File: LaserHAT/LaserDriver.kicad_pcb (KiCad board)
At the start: 2 copper layers, 65 x 56.9 mm, 69 parts, among them J1 GPIO, J2 Conn_02x02_Counter_Clockwise, J4 Jumper for 4-terminal diode c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, J5 USB_C_Receptacle_USB2.0_16P, J6 Conn_Coaxial, J7 Conn_Coaxial, Q1 SI3134KDWA-TP, Q2 DMN2056U, SW1 B, SW2 B, SW3 B, SW4 B, SW5 SW_SPDT, SW6 BSL, U1 CAT24C32, U2 MT3608, U3 TLV2371DBV, U4 MCP1700x-330xxMB, U5 AP2171W, U6 CH340N, U7 MSPM0G3507SRHBR

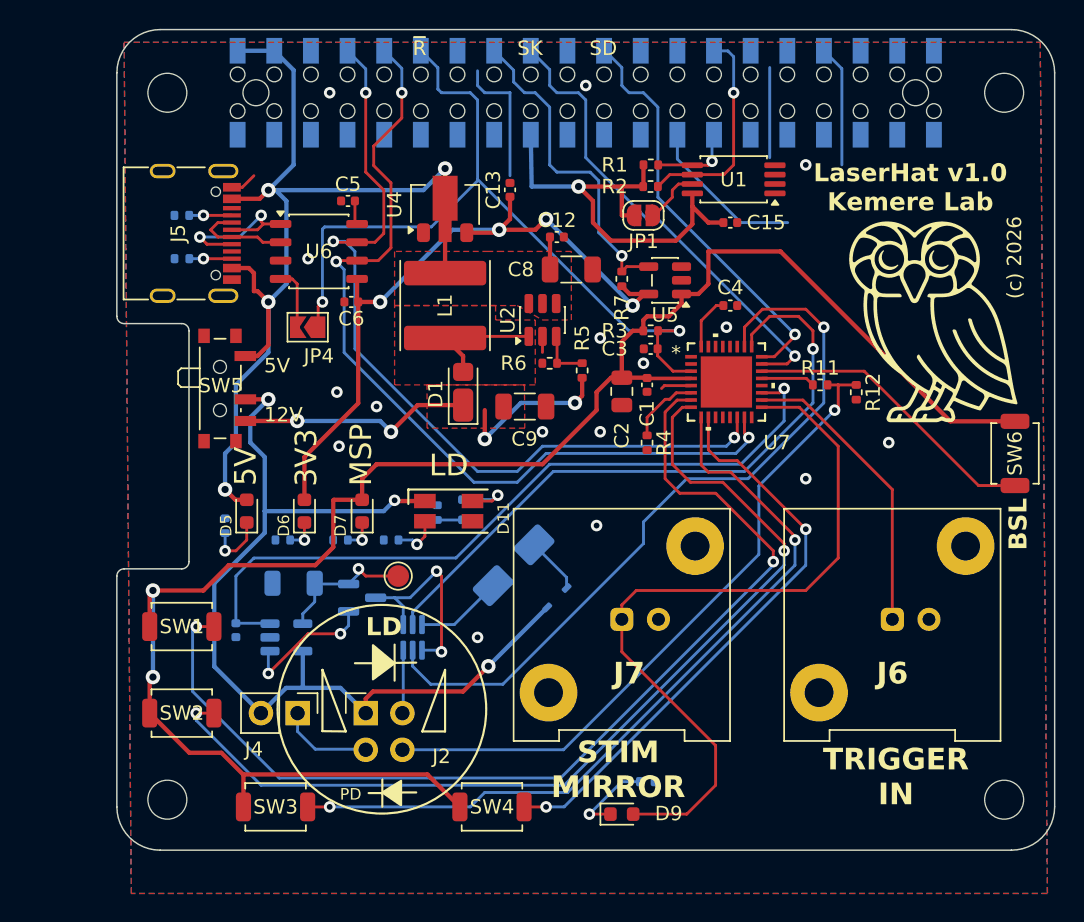
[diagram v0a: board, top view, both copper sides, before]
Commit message: LaserHAT Rev 2: hand-routed HAT, laser + e-stim daughterboards, fab outputs
HAT (LaserHAT/):
- Rev 1 -> Rev 2 schematic migration (tools/rev2_migrate.py): issue #3 fixes,
  OLED bonnet kept, analog stage moved to plug-in daughterboards (J8/J9),
  buffered BNC I/O, USB-C power switch + PFET ideal diode.
- MCU pin map re-optimised for fewest vias: Pi UART on UART1 (PA8/PA9), I2C on
  PA0/PA1 (fail-safe), PWM_A/B on TIMA0 CCP1/CCP3 (PA7/PA12) with FAULT0 on PA6,
  active-low buttons.  Pi header: SWD swapped, NRST <-> MCU_POWER_EN swapped.
- Stable symbol UUIDs so KiCad "Update PCB" never replaces footprints.
- PCB placed and routed by hand; tidied (tools/track_tidy.py), silkscreen
  decluttered (tools/silk_declutter.py).  DRC clean apart from known cosmetic items.
- JLC fab outputs regenerated (fab/LaserHAT).
- CLAUDE.md, REV2_NOTES.md updated; portable Claude memory in claude_memory/.

Daughterboards: LaserDaughter (300 mA laser driver) and EStimDaughter (isolated
e-stim, imported from kbest/estim_module); interface spec in estim_interface/.

Firmware/Pi: `make flash HAT_REV=2` selects the Rev 2 header wiring;
Pi/power_cycle.py takes its power/reset pins from the environment.

Co-Authored-By: Claude Opus 5.5 <noreply@anthropic.com>
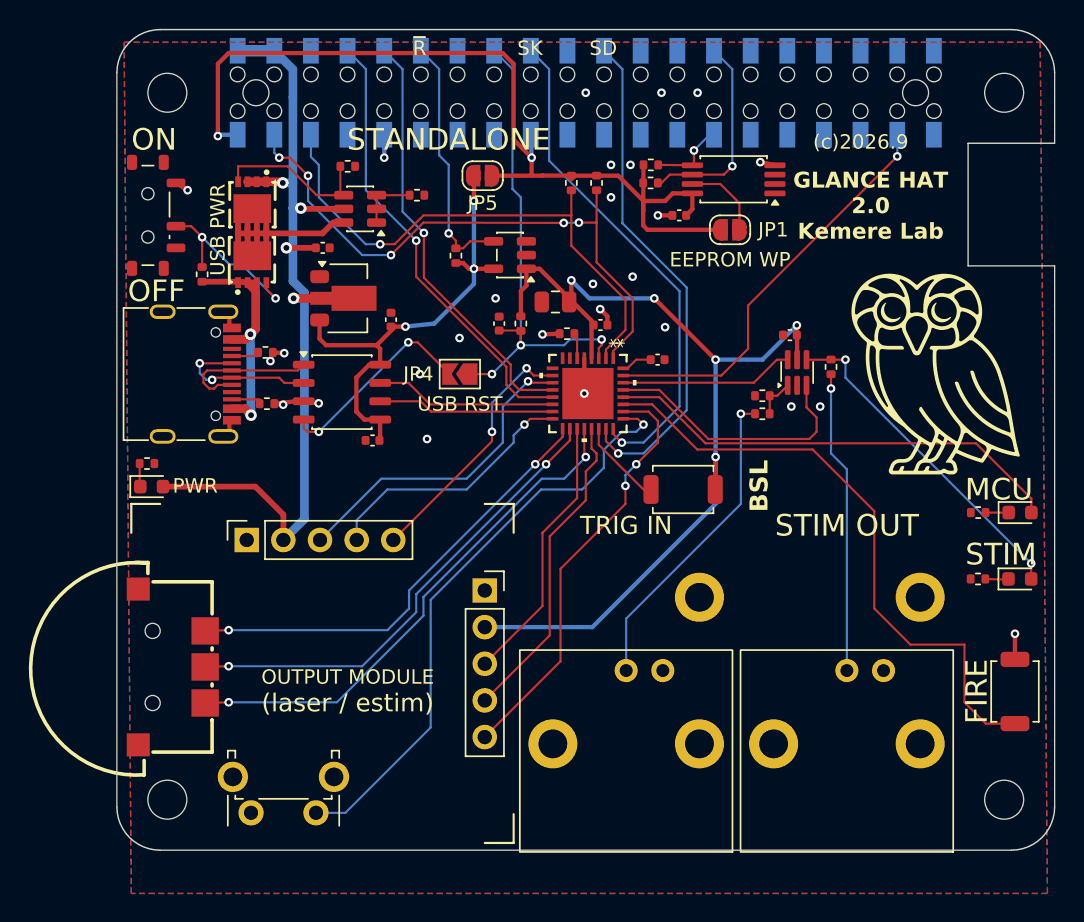
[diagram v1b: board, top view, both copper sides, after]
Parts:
- removed C11: 10nF, Capacitor_SMD:C_0402_1005Metric
- removed C5: 100nF, Capacitor_SMD:C_0402_1005Metric
- removed C8, C9: 22µF 16V, Capacitor_SMD:C_1206_3216Metric
- removed D1: SS14, Diode_SMD:D_SOD-123F
- removed D10: D_Zener 6.2V, Diode_SMD:D_SOD-523
- removed D11: LED_ABGR, LED_SMD:LED_RGB_1210
- removed D2: Zener 4.7V, 1.5W, Diode_SMD:D_SMA
- removed D3: 1N4148W, Footprints:D_SOD-323F
- removed D6: 3v3, Diode_SMD:D_0603_1608Metric
- removed J2: Conn_02x02_Counter_Clockwise, Connector_PinHeader_2.54mm:PinHeader_2x02_P2.54mm_Vertical
- removed J4: Jumper for 4-terminal diode configuration, Connector_PinHeader_2.54mm:PinHeader_1x02_P2.54mm_Vertical
- removed L1: 22uH, Inductor_SMD:L_APV_ANR6045
- removed Q2: DMN2056U, Package_TO_SOT_SMD:SOT-23
- removed R11: 1k 0.1%, Resistor_SMD:R_0402_1005Metric
- removed R12: 4.7k, Resistor_SMD:R_0402_1005Metric
- removed R14: 200, Resistor_SMD:R_0402_1005Metric
- removed R16: 470, Resistor_SMD:R_0402_1005Metric
- removed R17: 1k 1%, Resistor_SMD:R_0402_1005Metric
- removed R5: 187k 1%, Resistor_SMD:R_0402_1005Metric
- removed R6: 10k, Resistor_SMD:R_0402_1005Metric
- removed Rs1: 10Ω 1%, Resistor_SMD:R_1206_3216Metric
- removed SW1, SW3, SW4: B, Button_Switch_SMD:SW_SPST_TS-1088-xR020
- removed SW5: SW_SPDT, Button_Switch_SMD:SW_SPDT_PCM12
- removed TP1: TestPoint, TestPoint:TestPoint_Pad_D1.5mm
- removed U3: TLV2371DBV, Package_TO_SOT_SMD:SOT-23-5
- added C12: 100nF, Capacitor_SMD:C_0402_1005Metric, F.Cu at (114.3, 58.2)
- added J8: DB_POWER_TIMING, Connector_PinSocket_2.54mm:PinSocket_1x05_P2.54mm_Vertical, F.Cu at (109.0, 78.5)
- added J9: DB_ANALOG, Connector_PinSocket_2.54mm:PinSocket_1x05_P2.54mm_Vertical, F.Cu at (125.5, 82.0)
- added JP1: ID_WP, Jumper:SolderJumper-2_P1.3mm_Open_RoundedPad1.0x1.5mm, F.Cu at (142.5, 57.0)
- added Q3: AP30P30Q, Footprints:PDFN3333-8_PMOS_GSD, F.Cu at (109.4, 55.2)
- added Q5: AP30P30Q, Footprints:PDFN3333-8_PMOS_GSD, F.Cu at (109.4, 59.1)
- added R20: 4.7k, Resistor_SMD:R_0402_1005Metric, F.Cu at (131.5, 53.8)
- added R21: 47k, Resistor_SMD:R_0402_1005Metric, F.Cu at (120.8, 54.6)
- added R22: 10k, Resistor_SMD:R_0402_1005Metric, F.Cu at (116.0, 52.6)
- added R23: 1k, Resistor_SMD:R_0402_1005Metric, F.Cu at (144.7, 69.8)
- added R24: 100k, Resistor_SMD:R_0402_1005Metric, F.Cu at (144.7, 68.5)
- added R25: 33, Resistor_SMD:R_0402_1005Metric, F.Cu at (149.5, 66.5)
- added R26: 100k, Resistor_SMD:R_0402_1005Metric, F.Cu at (105.9, 60.1)
- added R3: 47k 1%, Resistor_SMD:R_0402_1005Metric, F.Cu at (128.0, 63.5)
- added SW10: USB PWR, Footprints:SW_SPDT_Shouhan_MSK12C02, F.Cu at (102.2, 56.0)
- added SW7: BL-DT (LCSC C53223909), Footprints:SW-SMD_BL-DT, F.Cu at (103.8, 87.3)
- added SW8: BACK, Button_Switch_THT:SW_Tactile_SPST_Angled_PTS645Vx39-2LFS, F.Cu at (113.8, 97.4)
- D7: value MSPM0 -> MCU
- J6: value Conn_Coaxial -> BNC TRIGGER IN; footprint Connector_Coaxial:BNC_Amphenol_031-5539_Vertical -> Footprints:BNC_Amphenol_031-5540_031-5539_Dual
- J7: value Conn_Coaxial -> BNC STIM OUT; footprint Connector_Coaxial:BNC_Amphenol_031-5539_Vertical -> Footprints:BNC_Amphenol_031-5540_031-5539_Dual
- JP4: value ID_WP -> RTS_NRST
- JP5: renamed from JP1; value ID_WP -> STANDALONE_3V3
- Q4: renamed from U2; value MT3608 -> DMMT5401
- R10, R8: moved to F.Cu
- R13: value 1k 1% -> 3k; moved to F.Cu
- R15: value 200 -> 2k; moved to F.Cu
- R18: value 470 -> 2k; moved to F.Cu
- R19: renamed from R3; value 47k 1% -> 4.7k
- SW9: renamed from SW2; value B -> FIRE
- U8: renamed from Q1; value SI3134KDWA-TP -> 74LVC2G17; moved to F.Cu
- moved SW9 57.8 mm to (162.2, 89.0), turned to 90 degrees
- moved D7 45.6 mm to (162.6, 76.6), turned to 0 degrees
- moved R15 44.2 mm to (159.7, 76.6)
- moved U8 32.4 mm to (147.2, 66.9)
- moved D9 32.0 mm to (162.6, 81.2)
- moved R18 26.9 mm to (159.7, 81.2), turned to 180 degrees
- moved SW6 23.1 mm to (139.2, 75.0), turned to 0 degrees
- moved J6 18.8 mm to (135.3, 87.5), turned to 180 degrees
- moved C16 17.5 mm to (146.7, 64.3), turned to 180 degrees
- moved J7 16.0 mm to (150.6, 87.5), turned to 180 degrees
- moved Q4 14.8 mm to (116.9, 55.5), turned to 180 degrees
- moved C13 12.2 mm to (119.0, 63.2)
- moved R10 11.6 mm to (110.4, 69.0), turned to 0 degrees
- moved R7 11.6 mm to (123.5, 58.8)
- moved JP5 11.5 mm to (125.3, 53.2), turned to 0 degrees
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- renumbered C12 to C16
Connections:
- net Net-(D9-K) renamed /BNC + Daughterboard I/O/STIM_LED_K
- C16 pad 1: +5V -> MSPM0_3V3
- C3 pad 1: /GPIO18/PCM.CLK -> /GPIO23
- D7 pad 2: MSPM0_3V3 -> LED_MCU
- D9 pad 2: /STIM_MIRROR -> /BNC + Daughterboard I/O/BUF_OUT
- J1 pad 10: /GPIO15/RXD0 -> PI_RXD
- J1 pad 3: /GPIO2/SDA1 -> I2C_SDA
- J1 pad 37: /GPIO26 -> PI_TRIGGER
- J1 pad 5: /GPIO3/SCL1 -> I2C_SCL
- J1 pad 8: /GPIO14/TXD0 -> PI_TXD
- J5 pad A4: +5V -> /USB-C UART/VBUS
- J5 pad A9: +5V -> /USB-C UART/VBUS
- J5 pad B4: +5V -> /USB-C UART/VBUS
- J5 pad B9: +5V -> /USB-C UART/VBUS
- J6 pad 1: /STIM_TRIGGER -> /BNC + Daughterboard I/O/BNC_IN
- J7 pad 1: /STIM_MIRROR -> /BNC + Daughterboard I/O/BNC_OUT
- JP4 pad 1: /GPIO18/PCM.CLK -> /GPIO23
- JP5 pad 1: Net-(JP1-A) -> +3V3
- Q4 pad 1: /Laser Driver Circuit/SW -> /USB-C UART/IDEAL_B
- Q4 pad 2: GND -> /USB-C UART/IDEAL_B
- Q4 pad 3: Net-(U2-FB) -> /USB-C UART/IDEAL_B
- Q4 pad 4: +5V -> /USB-C UART/IDEAL_G
- Q4 pad 6: unconnected-(U2-NC-Pad6) -> /USB-C UART/VBUS_SW
- R19 pad 1: MSPM0_3V3 -> RPi +3V3
- R19 pad 2: /GPIO18/PCM.CLK -> I2C_SDA
- R7 pad 2: /GPIO23 -> /GPIO18/PCM.CLK
- SW9 pad 1: /MSPM0 Controller/BUTTON2 -> /MSPM0 Controller/BUTTON5
- SW9 pad 2: MSPM0_3V3 -> GND
- U5 pad 4: /GPIO23 -> /GPIO18/PCM.CLK
- U6 pad 6: /GPIO15/RXD0 -> /MCU_UART_RX
- U6 pad 7: /GPIO14/TXD0 -> /MCU_UART_TX
- U6 pad 8: Net-(U6-V3) -> +3V3
- U7 pad 1: unconnected-(U7-PA0/FCC_IN-Pad1) -> I2C_SDA
- U7 pad 10: /MSPM0 Controller/BUTTON4 -> DB_GPIO
- U7 pad 11: unconnected-(U7-PA7/CLK_OUT-Pad11) -> DB_PWM_A
- U7 pad 12: unconnected-(U7-PA8-Pad12) -> PI_RXD
- U7 pad 13: unconnected-(U7-PA9/RTC_OUT/CLK_OUT-Pad13) -> PI_TXD
- U7 pad 14: /GPIO14/TXD0 -> /MCU_UART_TX
- U7 pad 15: /GPIO15/RXD0 -> /MCU_UART_RX
- U7 pad 16: unconnected-(U7-PA12/FCC_IN-Pad16) -> DB_PWM_B
- U7 pad 17: /STIM_MIRROR -> /MSPM0 Controller/BUTTON4
- U7 pad 18: /STIM_TRIGGER -> /MSPM0 Controller/BUTTON2
- U7 pad 19: /Laser Driver Circuit/LASER_VREF -> DB_DAC
- U7 pad 2: unconnected-(U7-PA1-Pad2) -> I2C_SCL
- U7 pad 20: unconnected-(U7-PA16/A1_1/FCC_IN-Pad20) -> /MSPM0 Controller/BUTTON3
- U7 pad 21: /Laser Driver Circuit/DIODE_ADC -> DB_ADC_A
- U7 pad 23: /GPIO24 -> /GPIO25
- U7 pad 24: /GPIO25 -> /GPIO24
- U7 pad 25: /Laser Driver Circuit/PWM_LASER -> /MSPM0 Controller/BUTTON1
- U7 pad 26: /Laser Driver Circuit/PWM_DUMMY -> DB_ADC_B
- U7 pad 27: unconnected-(U7-PA23/VREF+-Pad27) -> /MSPM0 Controller/BUTTON5
- U7 pad 28: unconnected-(U7-PA24/A0_3-Pad28) -> LED_MCU
- U7 pad 29: unconnected-(U7-PA25/A0_2/OPA0_IN1+-Pad29) -> MCU_STIM_OUT
- U7 pad 3: /GPIO18/PCM.CLK -> /GPIO23
- U7 pad 30: unconnected-(U7-PA26/A0_1-Pad30) -> MCU_STIM_IN
- U7 pad 31: unconnected-(U7-PA27/RTC_OUT/A0_0-Pad31) -> PI_TRIGGER
- U7 pad 33: unconnected-(U7-EPAD-Pad33) -> GND
- U7 pad 7: /MSPM0 Controller/BUTTON1 -> unconnected-(U7-PA3/COMP1_OUT/LFXIN-Pad7)
- U7 pad 8: /MSPM0 Controller/BUTTON2 -> unconnected-(U7-PA4/LFCLK_IN/LFXOUT-Pad8)
- U7 pad 9: /MSPM0 Controller/BUTTON3 -> unconnected-(U7-PA5/HFXIN/FCC_IN-Pad9)
- U8 pad 1: /Laser Driver Circuit/LaserDrive -> /BNC + Daughterboard I/O/BUF_IN
- U8 pad 2: /Laser Driver Circuit/PWM_DUMMY -> GND
- U8 pad 3: Net-(J2-LD_Cathode) -> MCU_STIM_OUT
- U8 pad 4: /Laser Driver Circuit/LaserDrive -> /BNC + Daughterboard I/O/BUF_OUT
- U8 pad 5: /Laser Driver Circuit/PWM_LASER -> MSPM0_3V3
- U8 pad 6: Net-(D2-K) -> MCU_STIM_IN
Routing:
- net LASER_V: track 66.0 -> 0.00 mm, vias 3 -> 0
- net /GPIO15/RXD0: track 60.9 -> 0.00 mm, vias 3 -> 0
- net /GPIO14/TXD0: track 58.3 -> 0.00 mm, vias 3 -> 0
- net MSPM0_3V3: track 123.9 -> 66.6 mm, vias 2 -> 5
- net /STIM_MIRROR: track 52.2 -> 0.00 mm
- net /Laser Driver Circuit/PWM_DUMMY: track 52.2 -> 0.00 mm, vias 1 -> 0
- net /Laser Driver Circuit/LASER_VREF: track 52.0 -> 0.00 mm, vias 1 -> 0
- net Net-(J2-PD_Anode): track 46.3 -> 0.00 mm, vias 1 -> 0
- net /Laser Driver Circuit/PWM_LASER: track 45.6 -> 0.00 mm, vias 1 -> 0
- net /MSPM0 Controller/BUTTON5: track 0.00 -> 42.6 mm
- net I2C_SDA: track 0.00 -> 41.7 mm, vias 0 -> 5
- net I2C_SCL: track 0.00 -> 38.0 mm, vias 0 -> 1
- net /GPIO18/PCM.CLK: track 55.2 -> 17.5 mm, vias 2 -> 1
- net /MSPM0 Controller/BUTTON2: track 67.0 -> 33.3 mm
- net RPi +3V3: track 31.2 -> 64.6 mm, vias 1 -> 2
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- removed copper zone on F.Cu, net +12V
- removed copper zone on F.Cu, net +5V
- removed copper zone on F.Cu, net /Laser Driver Circuit/SW
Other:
- outline, holes or cut-outs redrawn
- board text added: "(c)2026.9"
- board text added: "(laser / estim)"
- board text added: "EEPROM WP"
- board text added: "FIRE"
- board text added: "GLANCE HAT 2.0 Kemere Lab"
- board text added: "MCU"
- board text added: "OFF"
- board text added: "OLED BONNET (Adafruit 4567) 65 x 30.7 mm"
- board text added: "ON"
- board text added: "OUTPUT MODULE"
- board text added: "PWR"
- board text added: "Pi 4 PoE / Pi 5 fan"
- board text added: "STANDALONE"
- board text added: "STIM"
- board text added: "STIM OUT"
- board text added: "TRIG IN"
- board text added: "USB PWR"
- board text added: "USB RST"
- board text removed: "(c) 2026"
- board text removed: "12V"
- board text removed: "3V3"
- board text removed: "5V"
- board text removed: "LD"
- board text removed: "LaserHat v1.0 Kemere Lab"
- board text removed: "MSP"
- board text removed: "PD"
- board text removed: "STIM MIRROR"
- board text removed: "TRIGGER IN"

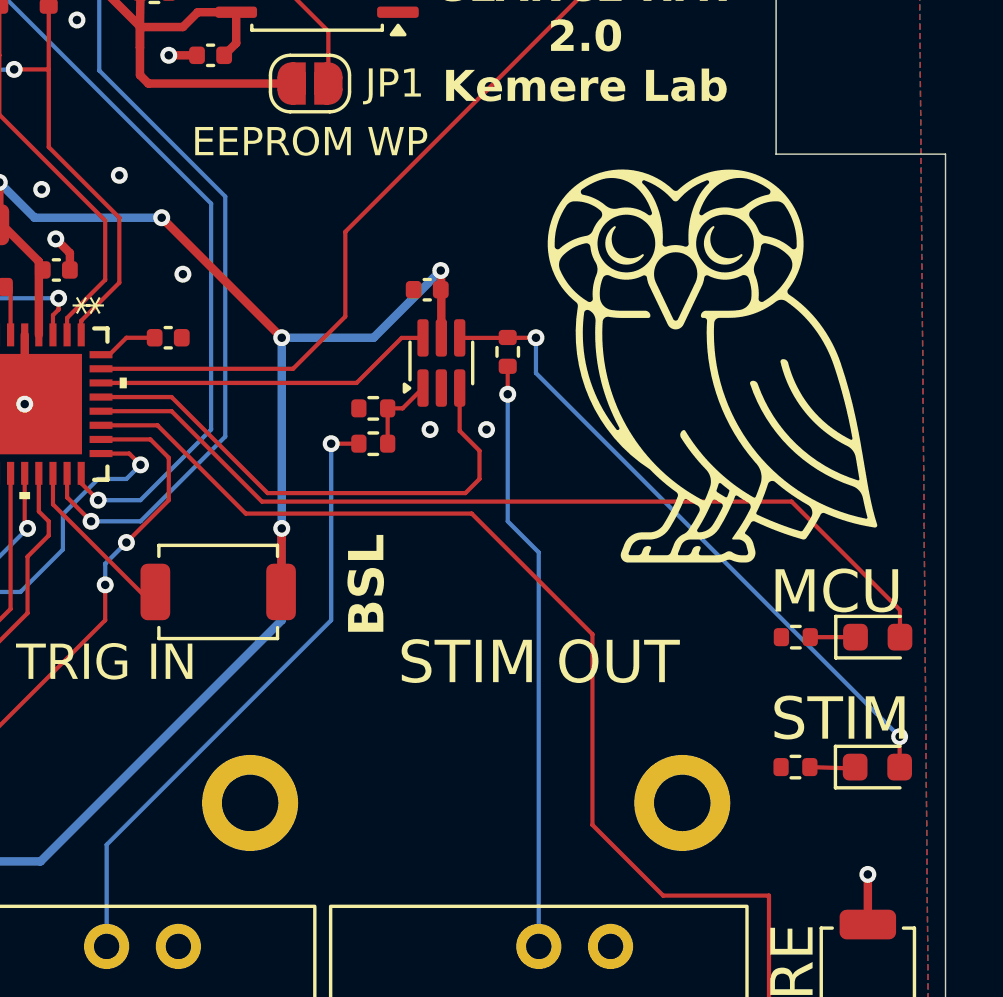
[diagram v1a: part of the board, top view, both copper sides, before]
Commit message: LaserHAT: new owl logo (OwlLogo_Laser_14mm) with a paired schematic symbol so it survives F8
- Footprints.pretty/OwlLogo_Laser_14mm: the new owl-with-laser-eyes artwork (parts/kicad/OwlLogo)
  scaled by 0.891 to the old logo's 13.9 mm height; silk lines clamped at 0.15 mm, filled
  polygons keep zero-width strokes, copper beams 0.27 mm.
- LaserHAT.kicad_sym: OwlLogo graphic symbol (no pins, not in BOM), footprint pre-assigned.
  Library format bumped to 20231120.
- LaserDriver.kicad_sch: symbol G1 on the root sheet; LaserDriver.kicad_pcb: the old REF**
  RICE_OWL_LOGO replaced by G1 at (155.8, 66.8), linked by path, excluded from BOM/CPL.
- DRC: no electrical items, schematic parity clean; the logo's own silk-over-copper and
  mask-bridge warnings are by design (plot with "subtract soldermask from silkscreen").

Co-Authored-By: Claude Fable 5.1 <noreply@anthropic.com>
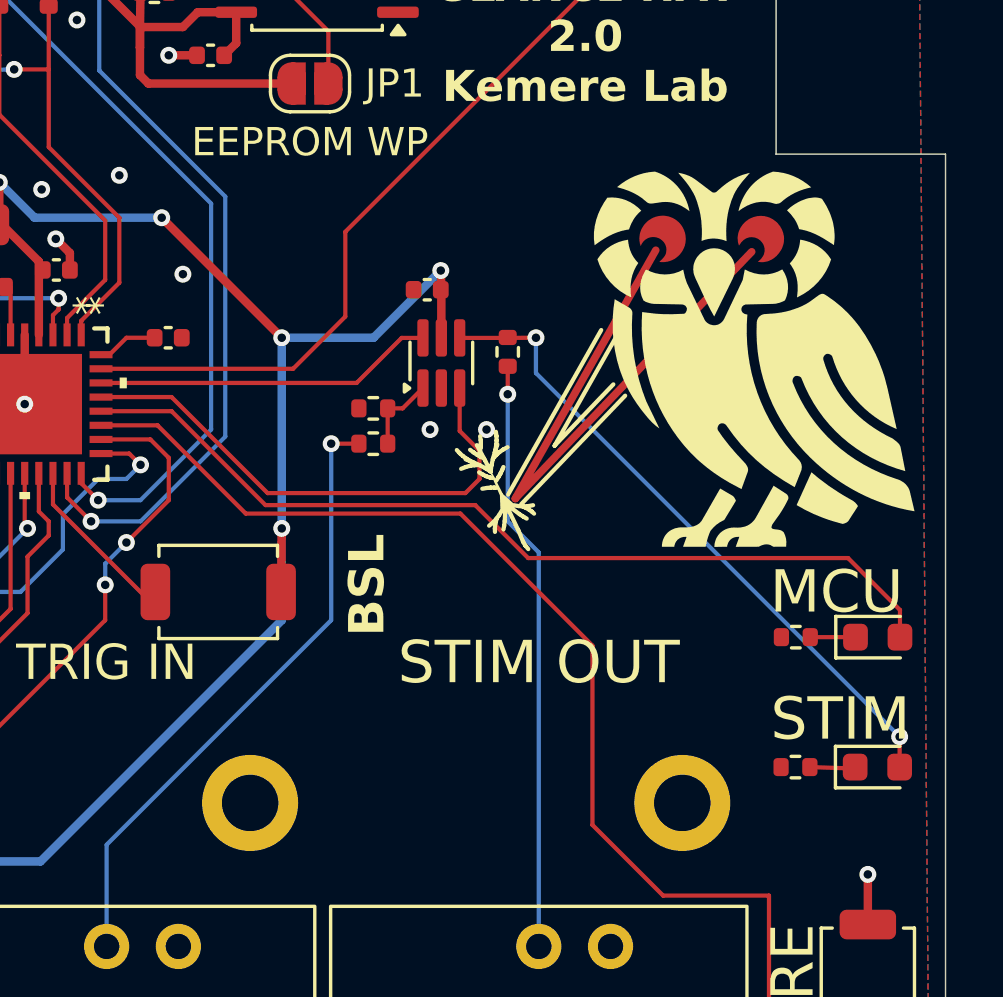
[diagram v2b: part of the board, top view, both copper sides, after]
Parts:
- removed REF**: RICE_OWL_LOGO, ELEC327-Kicad:RICE_OWL_LOGO
- added G1: OwlLogo, Footprints:OwlLogo_Laser_14mm, F.Cu at (155.8, 66.8)
